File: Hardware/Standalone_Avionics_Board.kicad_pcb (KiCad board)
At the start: 2 copper layers, 118.4 x 68.3 mm, 121 parts, among them J1 GPS_Ant, J2 Charges A/B Terminal, J3 Charges C/D Terminal, J4 RF_Ant, J5 10118192-0001LF, J6 ARM 10 Pin, Q1 SI1040X-T1-GE3, Q2 SI7232DN-T1-GE3, Q3 SI7232DN-T1-GE3, U1 Si4463, U10 LM317T, U11 USBLC6-2SC6, U12 STM32L562VET, U13 W25Q32JVSS, U2 Si4463, U3 RSD-897.500-942.500-1612-TR, U4 ADL5521, U5 MS5607-02BA, U6 MAX-8Q, U7 KX134-1211, U8 MCP9808_MSOP, U9 BNO055, Y1 30MHz, Y2 30MHz, Y3 32.768kHz, Y4 32MHz

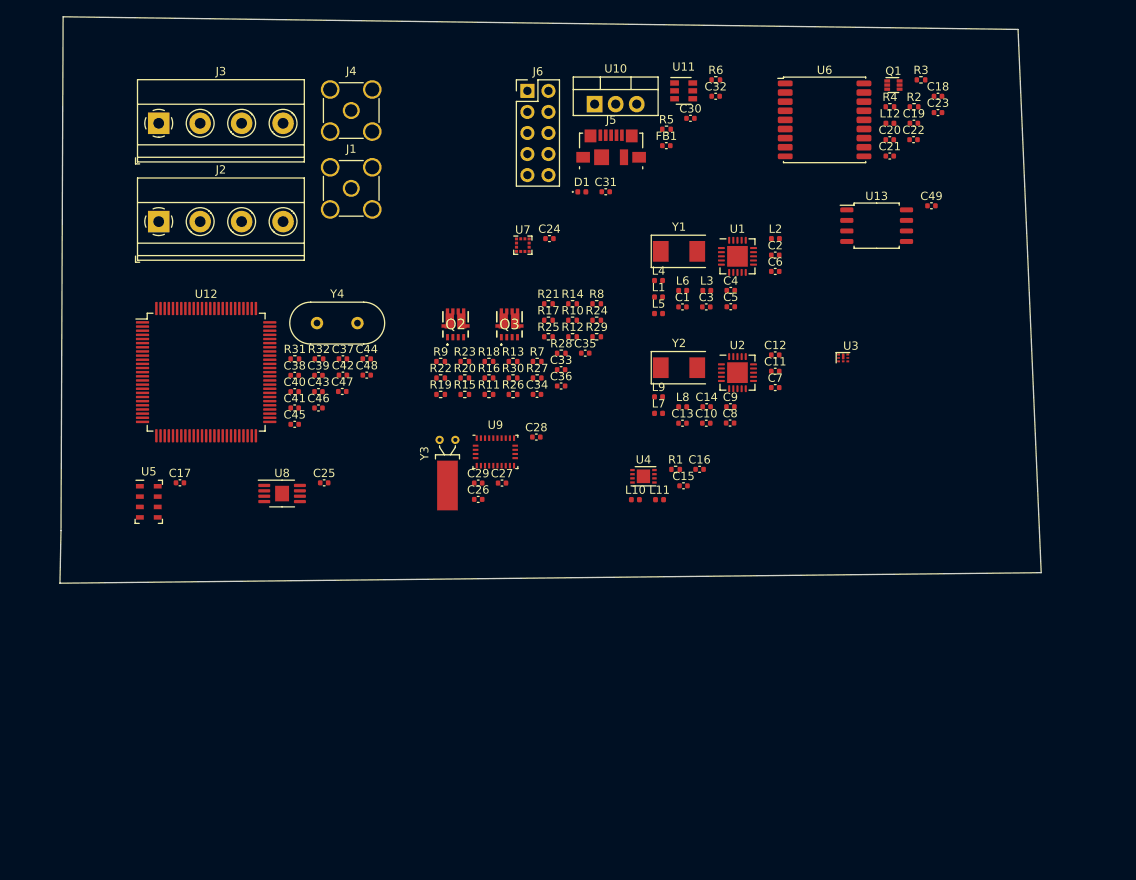
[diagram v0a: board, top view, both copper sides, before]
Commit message: Replaced 2x 4pole terminal blocks with 1x 8pole
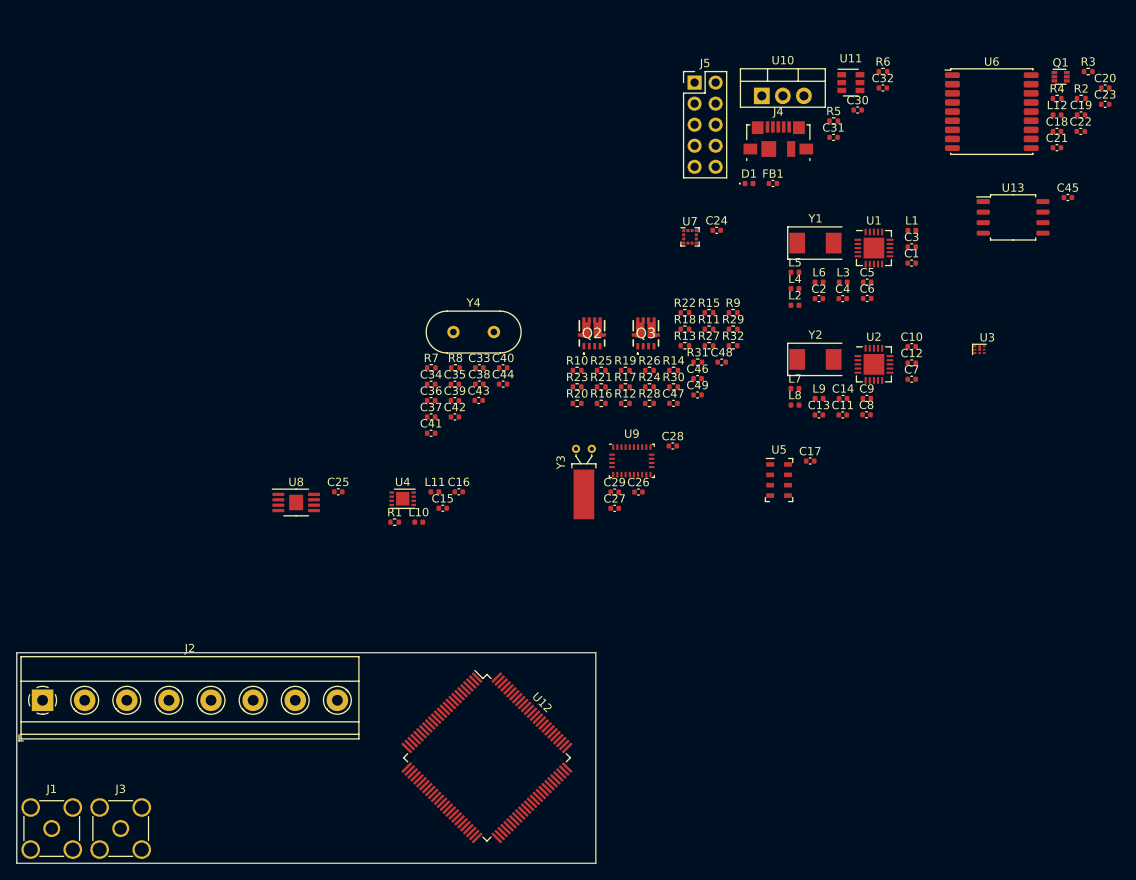
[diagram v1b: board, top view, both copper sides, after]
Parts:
- removed J6: ARM 10 Pin, Connector_PinHeader_2.54mm:PinHeader_2x05_P2.54mm_Vertical
- C33, C34: value CP1_Small -> 30pF
- C35: value CP1_Small -> 1uF
- C36: value CP1_Small -> 100nF
- C37, C38: value 30pF -> 100nF
- C39: value 1uF -> 100nF
- C46, C47, C48, C49: value 100nF -> CP1_Small
- J2: value Charges A/B Terminal -> Charges Terminal Block; footprint TerminalBlock_Phoenix:TerminalBlock_Phoenix_MKDS-1,5-4_1x04_P5.00mm_Horizontal -> TerminalBlock_Phoenix:TerminalBlock_Phoenix_MKDS-1,5-8-5.08_1x08_P5.08mm_Horizontal
- J3: value Charges C/D Terminal -> RF_Ant; footprint TerminalBlock_Phoenix:TerminalBlock_Phoenix_MKDS-1,5-4_1x04_P5.00mm_Horizontal -> Connector_Coaxial:SMA_Amphenol_132134-11_Vertical
- J4: value RF_Ant -> 10118192-0001LF; footprint Connector_Coaxial:SMA_Amphenol_132134-11_Vertical -> Connector_USB:USB_Micro-B_Molex_47346-0001
- J5: value 10118192-0001LF -> ARM 10 Pin; footprint Connector_USB:USB_Micro-B_Molex_47346-0001 -> Connector_PinHeader_2.54mm:PinHeader_2x05_P2.54mm_Vertical
- R11, R12: value 10k -> 1k
- R15, R16: value 10 -> 10k
- R17, R18, R21, R22: value 0.25 -> 10
- R19, R20: value 10 -> 0.25
- R23, R24: value 100k -> 0.25
- R27, R28: value 27k -> 100k
- R31, R32: value 4.7k -> 27k
- R7, R8: value 1k -> 4.7k
- moved C45 97.2 mm to (215.7, 84.8)
- moved J1 85.3 mm to (93.1, 160.9)
- moved J3 85.2 mm to (101.4, 160.9)
- moved C17 76.1 mm to (184.6, 116.6)
- moved U5 76.1 mm to (180.8, 118.9)
- moved J2 59.4 mm to (92.0, 145.4)
- moved U12 57.5 mm to (145.6, 152.4), turned to 315 degrees
- moved J4 51.6 mm to (180.8, 77.7)
- moved R32 50.0 mm to (175.3, 102.7)
- moved R31 48.6 mm to (171.0, 104.7)
- moved C46 45.9 mm to (171.0, 106.6)
- moved C48 42.8 mm to (173.9, 104.7)
- moved C47 40.0 mm to (168.1, 109.6)
- moved C49 36.3 mm to (171.0, 108.6)
- moved R9 35.8 mm to (175.3, 98.7)
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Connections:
- C35 pad 1: Net-(C35-Pad1) -> +3V3
- C36 pad 1: Net-(C36-Pad1) -> +3V3
- C37 pad 1: Net-(C37-Pad1) -> +3V3
- C38 pad 1: Net-(C38-Pad1) -> +3V3
- C46 pad 1: +3V3 -> Net-(C46-Pad1)
- C47 pad 1: +3V3 -> Net-(C47-Pad1)
- C48 pad 1: +3V3 -> Net-(C48-Pad1)
- C49 pad 1: +3V3 -> Net-(C49-Pad1)
- J3 pad 1: /Charges Firing Circuits/Fet_C+ -> /RSD DUPLEXER/Antenna
- J3 pad 2: /Charges Firing Circuits/Fet_C- -> GND
- J4 pad 1: /RSD DUPLEXER/Antenna -> Net-(FB1-Pad2)
- J4 pad 2: GND -> /USB, ESD, and Debug/USB_CONN_D-
- J5 pad 1: Net-(FB1-Pad2) -> +3V3
- J5 pad 2: /USB, ESD, and Debug/USB_CONN_D- -> /STM32L562VET6Q/DEBUG_SWDIO
- J5 pad 3: /USB, ESD, and Debug/USB_CONN_D+ -> GND
- J5 pad 4: Net-(J5-Pad4) -> /STM32L562VET6Q/DEBUG_SWCLK
- R10 pad 1: Net-(Q3-Pad4) -> Net-(Q2-Pad4)
- R10 pad 2: /Fire_D -> /Fire_B
- R11 pad 1: GND -> Net-(Q3-Pad2)
- R11 pad 2: Net-(Q2-Pad2) -> /Fire_C
- R12 pad 1: GND -> Net-(Q3-Pad4)
- R12 pad 2: Net-(Q2-Pad4) -> /Fire_D
- R13 pad 2: Net-(Q3-Pad2) -> Net-(Q2-Pad2)
- R14 pad 2: Net-(Q3-Pad4) -> Net-(Q2-Pad4)
- R15 pad 1: Net-(C33-Pad1) -> GND
- R15 pad 2: +5V -> Net-(Q3-Pad2)
- R16 pad 1: Net-(C34-Pad1) -> GND
- R16 pad 2: +5V -> Net-(Q3-Pad4)
- R17 pad 1: /Charges Firing Circuits/Fet_A- -> Net-(C46-Pad1)
- R17 pad 2: Net-(C33-Pad1) -> +5V
- R18 pad 1: /Charges Firing Circuits/Fet_B- -> Net-(C47-Pad1)
- R18 pad 2: Net-(C34-Pad1) -> +5V
- R19 pad 1: Net-(C35-Pad1) -> /Charges Firing Circuits/Fet_A-
- R19 pad 2: +5V -> Net-(C46-Pad1)
- R20 pad 1: Net-(C36-Pad1) -> /Charges Firing Circuits/Fet_B-
- R20 pad 2: +5V -> Net-(C47-Pad1)
- R21 pad 1: /Charges Firing Circuits/Fet_C- -> Net-(C48-Pad1)
- R21 pad 2: Net-(C35-Pad1) -> +5V
- R22 pad 1: /Charges Firing Circuits/Fet_D- -> Net-(C49-Pad1)
- R22 pad 2: Net-(C36-Pad1) -> +5V
- R23 pad 1: /Sense_A -> /Charges Firing Circuits/Fet_C-
- R23 pad 2: /Charges Firing Circuits/Fet_A+ -> Net-(C48-Pad1)
- R24 pad 1: /Sense_B -> /Charges Firing Circuits/Fet_D-
- R24 pad 2: /Charges Firing Circuits/Fet_B+ -> Net-(C49-Pad1)
- R25 pad 1: /Sense_C -> /Sense_A
- R25 pad 2: /Charges Firing Circuits/Fet_C+ -> /Charges Firing Circuits/Fet_A+
- R26 pad 1: /Sense_D -> /Sense_B
- R26 pad 2: /Charges Firing Circuits/Fet_D+ -> /Charges Firing Circuits/Fet_B+
- R27 pad 1: GND -> /Sense_C
- R27 pad 2: /Sense_A -> /Charges Firing Circuits/Fet_C+
- R28 pad 1: GND -> /Sense_D
- R28 pad 2: /Sense_B -> /Charges Firing Circuits/Fet_D+
- R29 pad 2: /Sense_C -> /Sense_A
- R30 pad 2: /Sense_D -> /Sense_B
- R31 pad 1: /SENSORS_I2C_SCL -> GND
- R31 pad 2: +3V3 -> /Sense_C
- R32 pad 1: /SENSORS_I2C_SDA -> GND
- R32 pad 2: +3V3 -> /Sense_D
- R7 pad 1: Net-(Q2-Pad2) -> /SENSORS_I2C_SCL
- R7 pad 2: /Fire_A -> +3V3
- R8 pad 1: Net-(Q2-Pad4) -> /SENSORS_I2C_SDA
- R8 pad 2: /Fire_B -> +3V3
- R9 pad 1: Net-(Q3-Pad2) -> Net-(Q2-Pad2)
- R9 pad 2: /Fire_C -> /Fire_A
- U12 pad 12: Net-(C37-Pad1) -> Net-(C33-Pad1)
- U12 pad 13: Net-(C38-Pad1) -> Net-(C34-Pad1)
- Y4 pad 1: Net-(C37-Pad1) -> Net-(C33-Pad1)
- Y4 pad 2: Net-(C38-Pad1) -> Net-(C34-Pad1)
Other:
- board size 118.4 x 68.3 mm -> 69.8 x 25.4 mm
- copper layers 2 -> 4

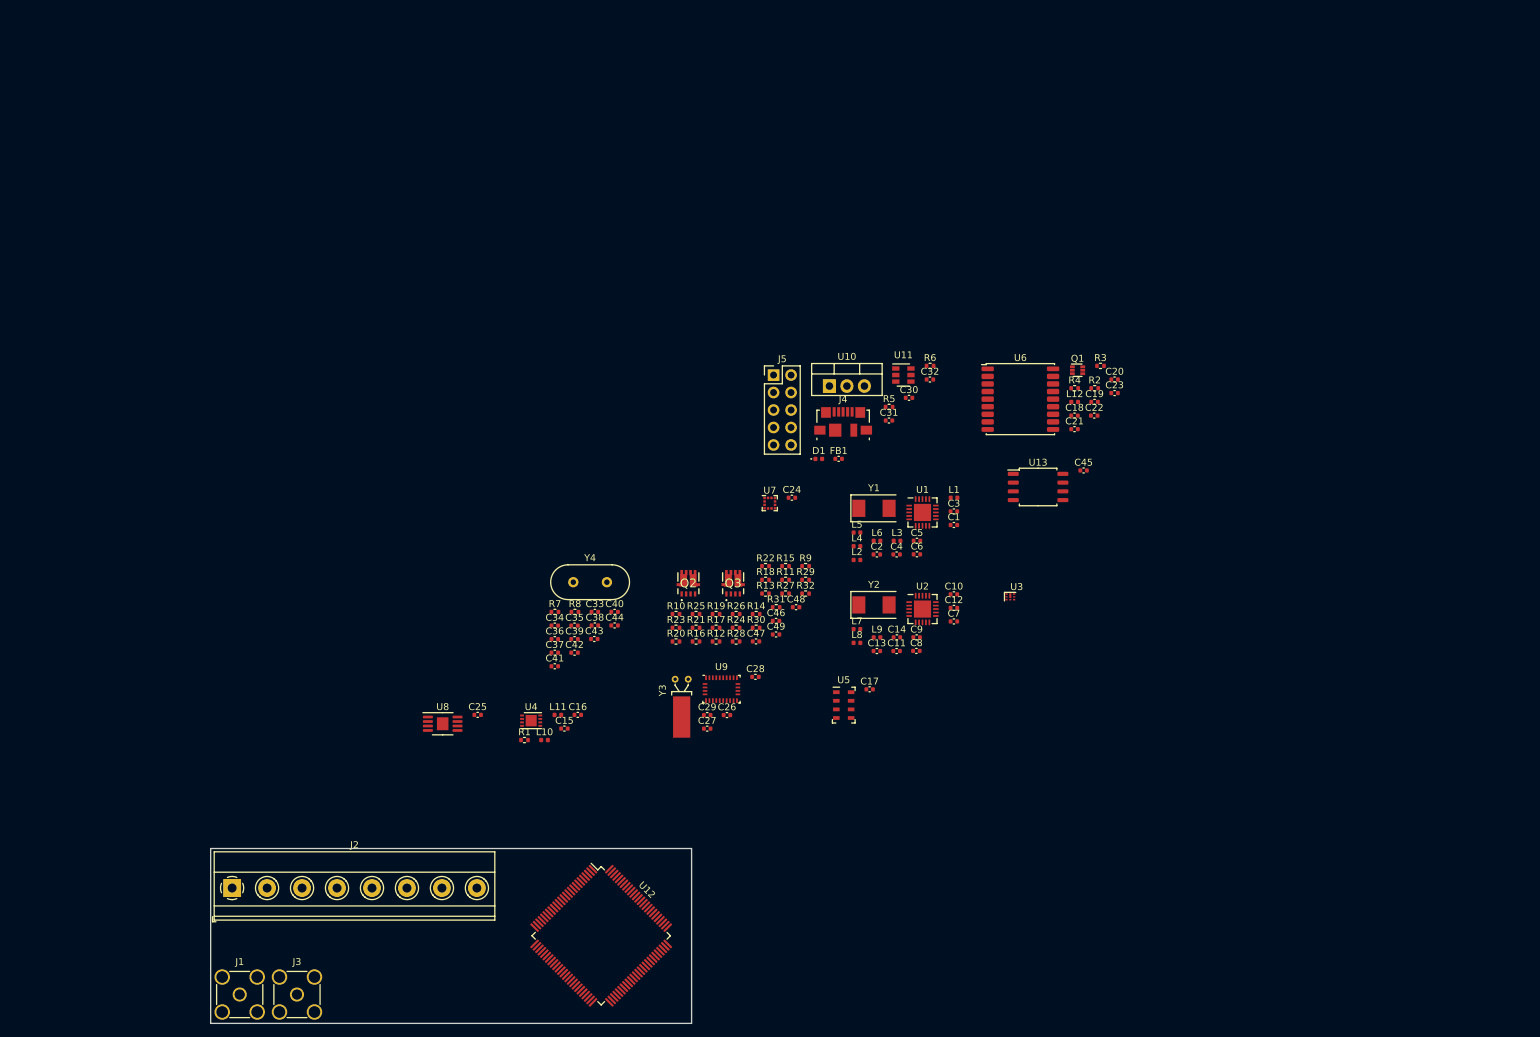
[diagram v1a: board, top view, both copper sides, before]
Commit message: Played with board sizes
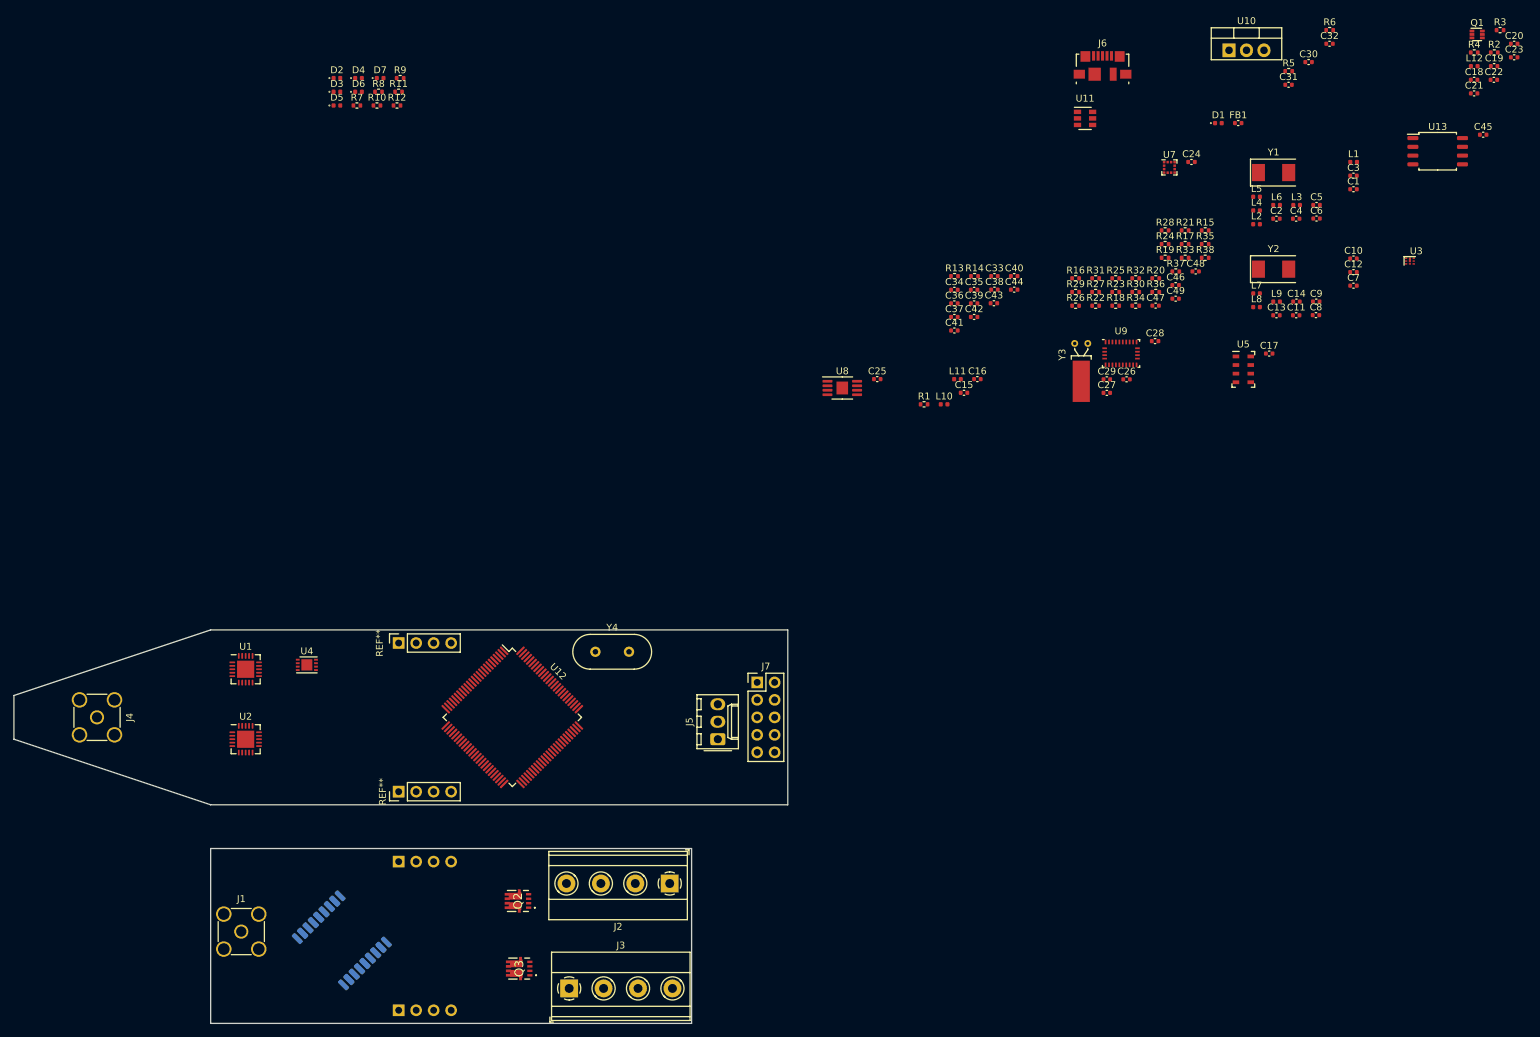
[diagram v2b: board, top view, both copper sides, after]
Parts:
- added D2: LED, LED_SMD:LED_0402_1005Metric, F.Cu at (107.2, 27.8)
- added D3: LED, LED_SMD:LED_0402_1005Metric, F.Cu at (107.2, 29.8)
- added D4: LED, LED_SMD:LED_0402_1005Metric, F.Cu at (110.4, 27.8)
- added D5: LED, LED_SMD:LED_0402_1005Metric, F.Cu at (107.2, 31.8)
- added D6: LED, LED_SMD:LED_0402_1005Metric, F.Cu at (110.4, 29.8)
- added D7: LED, LED_SMD:LED_0402_1005Metric, F.Cu at (113.5, 27.8)
- added J3: Charges C/D Terminal, TerminalBlock_Phoenix:TerminalBlock_Phoenix_MKDS-1,5-4_1x04_P5.00mm_Horizontal, F.Cu at (141.0, 160.0)
- added J5: 3-Pin Molex Power, Connector_Molex:Molex_KK-254_AE-6410-03A_1x03_P2.54mm_Vertical, F.Cu at (162.6, 123.8)
- added R10: 100Ω, Resistor_SMD:R_0402_1005Metric, F.Cu at (113.1, 31.8)
- added R11: 100Ω, Resistor_SMD:R_0402_1005Metric, F.Cu at (116.2, 29.8)
- added R12: 100Ω, Resistor_SMD:R_0402_1005Metric, F.Cu at (116.0, 31.8)
- added R7: 100Ω, Resistor_SMD:R_0402_1005Metric, F.Cu at (110.1, 31.8)
- added R8: 100Ω, Resistor_SMD:R_0402_1005Metric, F.Cu at (113.3, 29.8)
- added R9: 100Ω, Resistor_SMD:R_0402_1005Metric, F.Cu at (116.4, 27.8)
- added REF**: PinHeader_1x04_P2.54mm_Vertical, Connector_PinHeader_2.54mm:PinHeader_1x04_P2.54mm_Vertical, B.Cu at (116.2, 163.2)
- added REF**: PinSocket_1x04_P2.54mm_Vertical, Connector_PinSocket_2.54mm:PinSocket_1x04_P2.54mm_Vertical, F.Cu at (116.2, 109.9)
- added REF**: PinSocket_1x04_P2.54mm_Vertical, Connector_PinSocket_2.54mm:PinSocket_1x04_P2.54mm_Vertical, B.Cu at (116.2, 141.6)
- added REF**: PinHeader_1x04_P2.54mm_Vertical, Connector_PinHeader_2.54mm:PinHeader_1x04_P2.54mm_Vertical, F.Cu at (116.2, 131.4)
- J2: value Charges Terminal Block -> Charges A/B Terminal; footprint TerminalBlock_Phoenix:TerminalBlock_Phoenix_MKDS-1,5-8-5.08_1x08_P5.08mm_Horizontal -> TerminalBlock_Phoenix:TerminalBlock_Phoenix_MKDS-1,5-4_1x04_P5.00mm_Horizontal
- U6: moved to B.Cu
- moved U6 126.1 mm to (108.0, 153.0), turned to 135 degrees
- moved U1 100.9 mm to (94.0, 113.7)
- moved U2 100.1 mm to (94.0, 123.8)
- moved C31 75.8 mm to (245.5, 28.8)
- moved C36 75.8 mm to (196.9, 60.5)
- moved C37 75.8 mm to (196.9, 62.5)
- moved R20 75.8 mm to (226.2, 56.9)
- moved C1 75.8 mm to (254.9, 43.9)
- moved C10 75.8 mm to (254.9, 54.0)
- moved C12 75.8 mm to (254.9, 56.0)
- moved C13 75.8 mm to (243.7, 62.3)
- moved C14 75.8 mm to (246.6, 60.3)
- moved C19 75.8 mm to (275.3, 26.1)
- moved C2 75.8 mm to (243.7, 48.2)
- moved C21 75.8 mm to (272.4, 30.0)
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- renumbered J3 to J4, J4 to J6, J5 to J7, R7 to R13, R8 to R14, R9 to R15, R10 to R16, R11 to R17, R12 to R18, R13 to R19, R14 to R20, R15 to R21, R16 to R22, R17 to R23, R18 to R24, R19 to R25, R20 to R26, R21 to R27, R22 to R28, R23 to R29, R24 to R30, R25 to R31, R26 to R32, R27 to R33, R28 to R34, R29 to R35, R30 to R36, R31 to R37, R32 to R38
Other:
- board size 69.8 x 25.4 mm -> 112.4 x 57.1 mm
